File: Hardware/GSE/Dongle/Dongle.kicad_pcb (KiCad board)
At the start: 2 copper layers, 16 parts, among them J1 USB_A, J2 Conn_Coaxial, J3 USB_A, U1 XBee_SMT, U2 FT231XS, U3 AP2114H-3.3TRG1

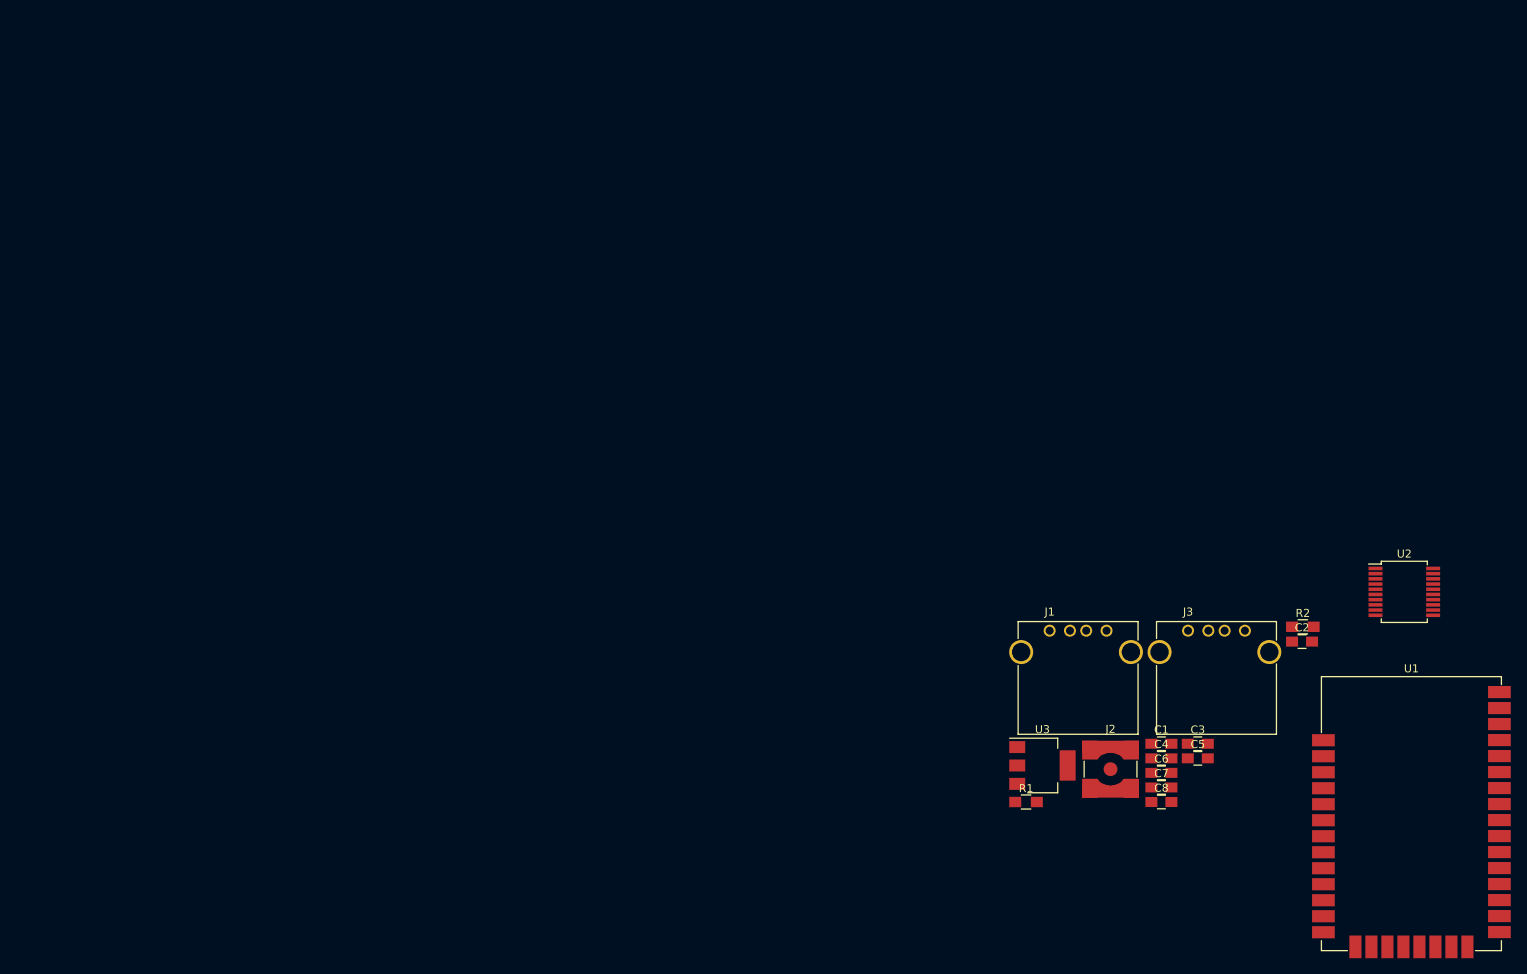
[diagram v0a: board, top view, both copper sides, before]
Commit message: prelim dongle routing
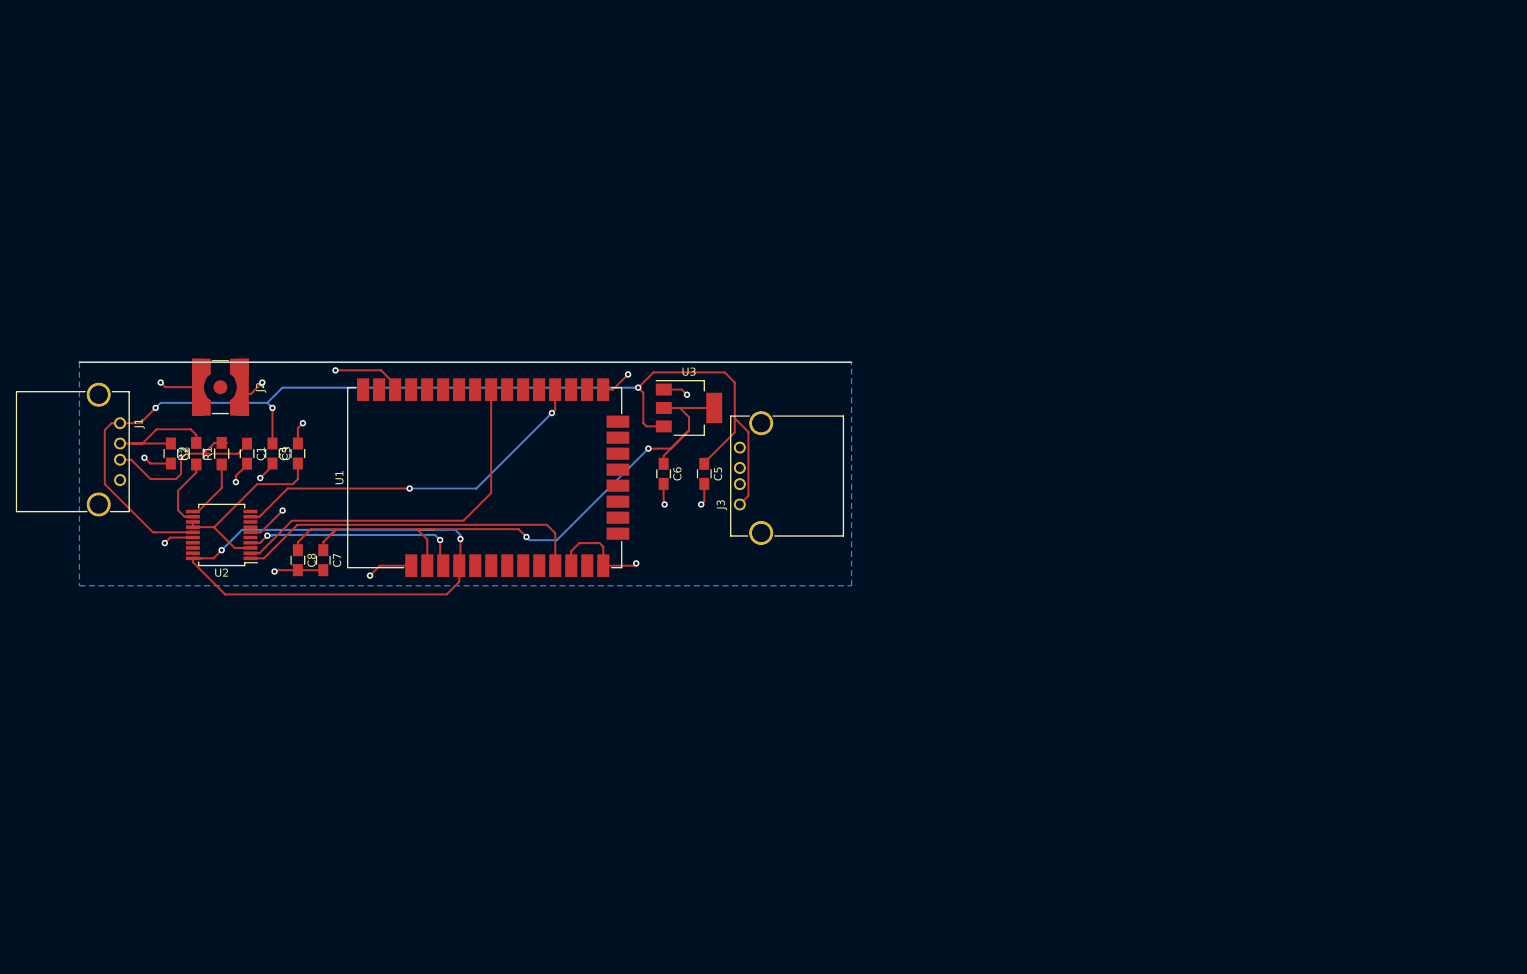
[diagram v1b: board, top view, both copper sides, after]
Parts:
- moved U2 148.0 mm to (17.8, 64.8), turned to 180 degrees
- moved C2 143.3 mm to (11.4, 54.6), turned to 270 degrees
- moved R2 140.0 mm to (14.6, 54.6), turned to 90 degrees
- moved U1 122.8 mm to (51.4, 57.6), turned to 90 degrees
- moved C3 121.2 mm to (24.1, 54.6), turned to 270 degrees
- moved J2 121.1 mm to (17.6, 46.3), turned to 270 degrees
- moved C1 119.9 mm to (21.0, 54.6), turned to 270 degrees
- moved J1 119.1 mm to (5.08, 50.8), turned to 270 degrees
- moved C4 114.5 mm to (27.3, 54.6), turned to 90 degrees
- moved C8 112.1 mm to (27.3, 67.9), turned to 270 degrees
- moved R1 109.6 mm to (17.8, 54.6), turned to 90 degrees
- moved C7 108.5 mm to (30.5, 67.9), turned to 270 degrees
- moved C6 72.6 mm to (73.0, 57.1), turned to 270 degrees
- moved C5 71.2 mm to (78.1, 57.1), turned to 270 degrees
- moved U3 62.8 mm to (76.2, 48.9)
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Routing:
- net 5V: track 0.00 -> 139.1 mm, vias 0 -> 3
- net Net-(C6-Pad1): track 0.00 -> 83.7 mm, vias 0 -> 2
- net DIN: track 0.00 -> 78.3 mm, vias 0 -> 2
- net GND: track 0.00 -> 76.2 mm, vias 0 -> 16
- net CTS: track 0.00 -> 46.1 mm, vias 0 -> 2
- net RTS: track 0.00 -> 46.1 mm
- net DTR: track 0.00 -> 44.3 mm
- net DOUT: track 0.00 -> 27.7 mm, vias 0 -> 2
- net Net-(C4-Pad1): track 0.00 -> 23.9 mm
- net Net-(C1-Pad1): track 0.00 -> 23.4 mm
- net Net-(C2-Pad1): track 0.00 -> 16.5 mm
- net Net-(R2-Pad1): track 0.00 -> 8.85 mm
- net Net-(R1-Pad1): track 0.00 -> 7.76 mm
- added copper zone on B.Cu, net GND

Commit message: GSE dongle layout
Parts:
- added G***: LOGO, Logos:logo6, B.Cu at (34.3, 17.1)
- added REF**: MountingHole_3.2mm_M3_Pad, Mounting_Holes:MountingHole_3.2mm_M3_Pad, F.Cu at (4.00, 4.00)
- added REF**: MountingHole_3.2mm_M3_Pad, Mounting_Holes:MountingHole_3.2mm_M3_Pad, F.Cu at (4.00, 29.0)
- added REF**: MountingHole_3.2mm_M3_Pad, Mounting_Holes:MountingHole_3.2mm_M3_Pad, F.Cu at (86.0, 29.0)
- added REF**: MountingHole_3.2mm_M3_Pad, Mounting_Holes:MountingHole_3.2mm_M3_Pad, F.Cu at (86.0, 4.00)
- J2: footprint Connectors:SMA_SMD_Jack_Straight -> Connectors_Molex:Molex_SMA_Jack_Edge_Mount
- J3: value USB_A -> Conn_01x02_Male; footprint Connectors:USB_A -> Payload2019_Connectors:Molex_KK_1718570002
- moved C5 62.4 mm to (33.0, 13.9), turned to 90 degrees
- moved C6 55.5 mm to (38.1, 13.9), turned to 90 degrees
- moved U3 54.1 mm to (27.9, 24.5)
- moved R1 48.3 mm to (17.8, 6.27)
- moved R2 48.2 mm to (12.7, 6.43), turned to 270 degrees
- moved J3 45.7 mm to (83.8, 15.2), turned to 270 degrees
- moved C7 44.4 mm to (40.6, 24.7)
- moved C8 44.0 mm to (35.6, 24.7)
- moved J2 44.0 mm to (30.5, 4.26)
- moved U1 42.2 mm to (61.0, 16.5)
- moved C4 40.8 mm to (22.9, 14.0)
- moved C3 40.8 mm to (27.9, 14.0)
- moved C1 40.7 mm to (17.8, 14.0), turned to 90 degrees
- moved C2 40.7 mm to (12.7, 13.9), turned to 90 degrees
- moved U2 40.2 mm to (14.0, 24.8)
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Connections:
- J3 pad 2: Net-(J3-Pad2) -> GND
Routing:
- net RTS: track 46.1 -> 117.7 mm, vias 0 -> 2
- net CTS: track 46.1 -> 104.9 mm
- net Net-(J2-Pad1): track 0.00 -> 30.6 mm
- net Net-(C6-Pad1): track 83.7 -> 54.3 mm
- net DIN: track 78.3 -> 51.9 mm, vias 2 -> 0
- net DOUT: track 27.7 -> 53.5 mm, vias 2 -> 0
- net Net-(R1-Pad1): track 7.76 -> 22.6 mm
- net 5V: track 139.1 -> 152.1 mm, vias 3 -> 2
- net DTR: track 44.3 -> 56.4 mm, vias 0 -> 2
- net Net-(R2-Pad1): track 8.85 -> 20.8 mm, vias 0 -> 2
- net GND: track 76.2 -> 65.6 mm, vias 16 -> 15
- net Net-(C1-Pad1): track 23.4 -> 26.2 mm
- net Net-(C2-Pad1): track 16.5 -> 17.4 mm
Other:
- board outline added: 90 x 33 mm
- board text added: "0.6mm thickness, 4.4 permeability"
- board text added: ":partyparrot: rev1 2018"

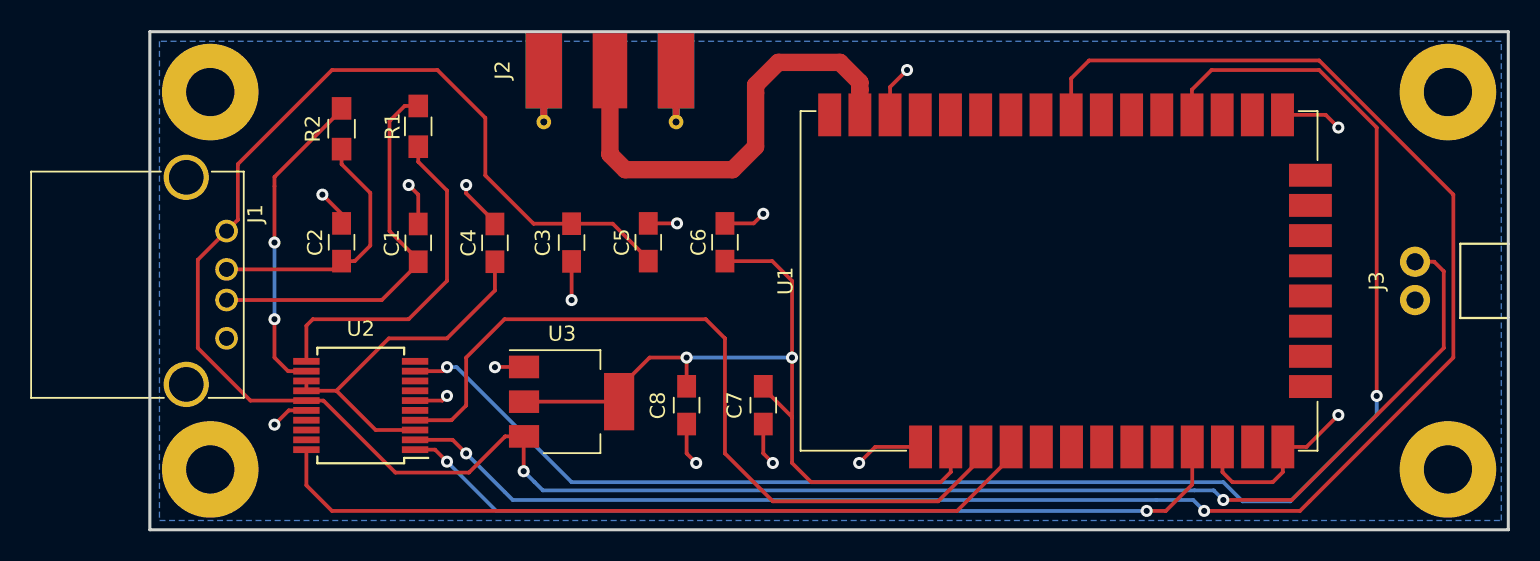
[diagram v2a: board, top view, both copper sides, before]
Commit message: new connectors for GSE board
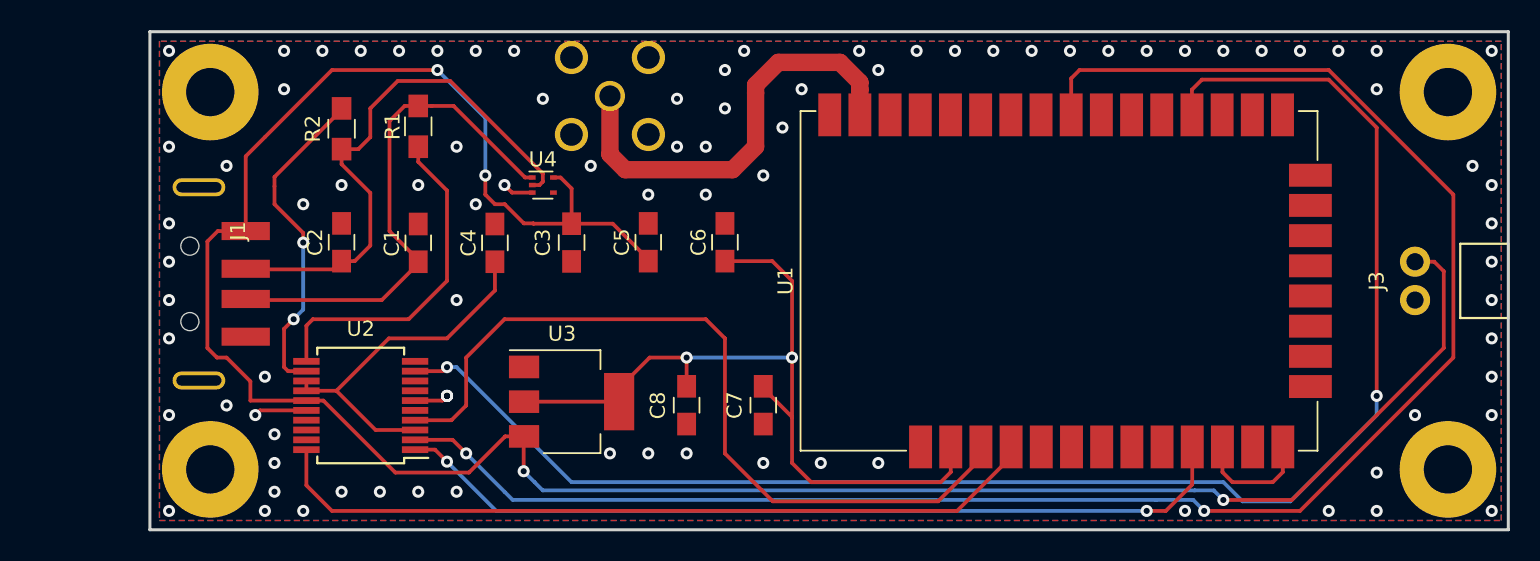
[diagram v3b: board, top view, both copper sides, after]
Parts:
- added U4: TPD3E001DRLR, TO_SOT_Packages_SMD:SOT-553, F.Cu at (26.0, 10.2)
- J1: footprint Connectors:USB_A -> Payload2019_Connectors:629104151021
- J2: footprint Connectors_Molex:Molex_SMA_Jack_Edge_Mount -> Payload2019_Connectors:CONSMA002
- moved J1 1.27 mm to (6.35, 13.2)
- moved G*** 0.64 mm to (34.3, 17.8)
- turned J2 to 0 degrees
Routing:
- net GND: track 65.6 -> 15.7 mm, vias 15 -> 86
- net Net-(C2-Pad1): track 17.4 -> 37.5 mm
- net Net-(C1-Pad1): track 26.2 -> 35.8 mm
- net 5V: track 152.1 -> 157.6 mm, vias 2 -> 4
- net Net-(J2-Pad1): track 30.6 -> 28.9 mm
- net Net-(R2-Pad1): track 20.8 -> 21.9 mm
- net RTS: track 117.7 -> 117.1 mm
- net CTS: track 104.9 -> 104.4 mm
- net (no net): vias 0 -> 4
- added copper zone on F.Cu, net GND
